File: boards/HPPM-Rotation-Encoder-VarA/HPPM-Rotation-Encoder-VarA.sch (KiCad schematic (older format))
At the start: 13 parts, among them J1 CONN, U1 AS5045B, U2 DS9638

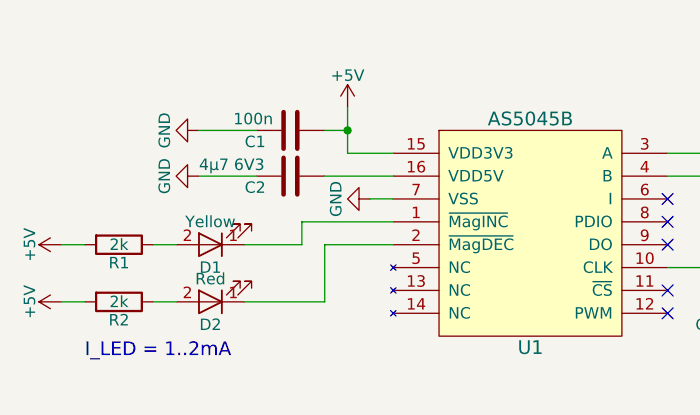
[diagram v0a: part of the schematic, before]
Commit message: [board][HPPM-Rotation-Encoder-VarA] fix wrong pinout
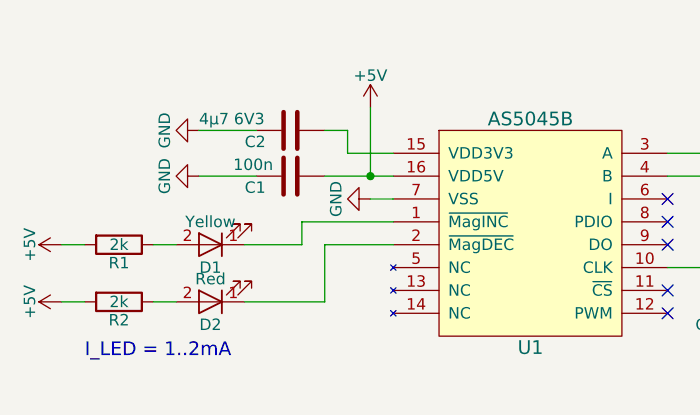
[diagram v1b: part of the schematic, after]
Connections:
- net +5V: now also U1.16 (VDD5V); no longer U1.15 (VDD3V3)
- net at C2.1: now also U1.15 (VDD3V3); no longer U1.16 (VDD5V)
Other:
- moved on the sheet: C1, C2
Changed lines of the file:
@@
 LIBS:ds9638
 LIBS:as5045b
+LIBS:HPPM-Rotation-Encoder-VarA-cache
 EELAYER 25 0
 EELAYER END
@@
 L +5V #PWR01
 U 1 1 5B107E82
-P 4800 3150
-F 0 "#PWR01" H 4800 3000 50  0001 C CNN
-F 1 "+5V" H 4800 3290 50  0000 C CNN
-F 2 "" H 4800 3150 50  0001 C CNN
-F 3 "" H 4800 3150 50  0001 C CNN
-	1    4800 3150
-	1    0    0    -1
-$EndComp
-Wire Wire Line
-	5000 3350 4800 3350
-Wire Wire Line
-	4800 3350 4800 3150
+P 4900 3150
+F 0 "#PWR01" H 4900 3000 50  0001 C CNN
+F 1 "+5V" H 4900 3290 50  0000 C CNN
+F 2 "" H 4900 3150 50  0001 C CNN
+F 3 "" H 4900 3150 50  0001 C CNN
+	1    4900 3150
+	1    0    0    -1
+$EndComp
 $Comp
 L GND #PWR02
@@
 L C C1
 U 1 1 5B107F98
+P 4550 3450
+F 0 "C1" V 4600 3250 50  0000 L CNN
+F 1 "100n" V 4500 3200 50  0000 L CNN
+F 2 "Capacitors_SMD:C_0603" H 4588 3300 50  0001 C CNN
+F 3 "" H 4550 3450 50  0001 C CNN
+	1    4550 3450
+	0    1    1    0
+$EndComp
+$Comp
+L GND #PWR03
+U 1 1 5B1080A9
+P 4150 3450
+F 0 "#PWR03" H 4150 3200 50  0001 C CNN
+F 1 "GND" H 4150 3300 50  0000 C CNN
+F 2 "" H 4150 3450 50  0001 C CNN
+F 3 "" H 4150 3450 50  0001 C CNN
+	1    4150 3450
+	0    1    1    0
+$EndComp
+Wire Wire Line
+	4900 3550 5000 3550
+$Comp
+L C C2
+U 1 1 5B1080D6
 P 4550 3250
-F 0 "C1" V 4600 3050 50  0000 L CNN
-F 1 "100n" V 4500 3000 50  0000 L CNN
+F 0 "C2" V 4600 3050 50  0000 L CNN
+F 1 "4µ7 6V3" V 4500 2850 50  0000 L CNN
 F 2 "Capacitors_SMD:C_0603" H 4588 3100 50  0001 C CNN
 F 3 "" H 4550 3250 50  0001 C CNN
@@
 $EndComp
 $Comp
-L GND #PWR03
-U 1 1 5B1080A9
+L GND #PWR04
+U 1 1 5B10817D
 P 4150 3250
-F 0 "#PWR03" H 4150 3000 50  0001 C CNN
+F 0 "#PWR04" H 4150 3000 50  0001 C CNN
 F 1 "GND" H 4150 3100 50  0000 C CNN
 F 2 "" H 4150 3250 50  0001 C CNN
@@
 $EndComp
 Wire Wire Line
-	4900 3550 5000 3550
-$Comp
-L C C2
-U 1 1 5B1080D6
-P 4550 3450
-F 0 "C2" V 4600 3250 50  0000 L CNN
-F 1 "4µ7 6V3" V 4500 3050 50  0000 L CNN
-F 2 "Capacitors_SMD:C_0603" H 4588 3300 50  0001 C CNN
-F 3 "" H 4550 3450 50  0001 C CNN
-	1    4550 3450
-	0    1    1    0
-$EndComp
-$Comp
-L GND #PWR04
-U 1 1 5B10817D
-P 4150 3450
-F 0 "#PWR04" H 4150 3200 50  0001 C CNN
-F 1 "GND" H 4150 3300 50  0000 C CNN
-F 2 "" H 4150 3450 50  0001 C CNN
-F 3 "" H 4150 3450 50  0001 C CNN
-	1    4150 3450
-	0    1    1    0
-$EndComp
+	4150 3250 4400 3250
 Wire Wire Line
 	4150 3450 4400 3450
-Wire Wire Line
-	4150 3250 4400 3250
-Wire Wire Line
-	4700 3250 4800 3250
-Connection ~ 4800 3250
-Wire Wire Line
-	4700 3450 5000 3450
 $Comp
 L C C4
@@
 Wire Wire Line
 	9250 3050 9250 2950
+Wire Wire Line
+	4700 3450 5000 3450
+Wire Wire Line
+	5000 3350 4800 3350
+Wire Wire Line
+	4800 3350 4800 3250
+Wire Wire Line
+	4800 3250 4700 3250
+Wire Wire Line
+	4900 3150 4900 3450
+Connection ~ 4900 3450
 $EndSCHEMATC

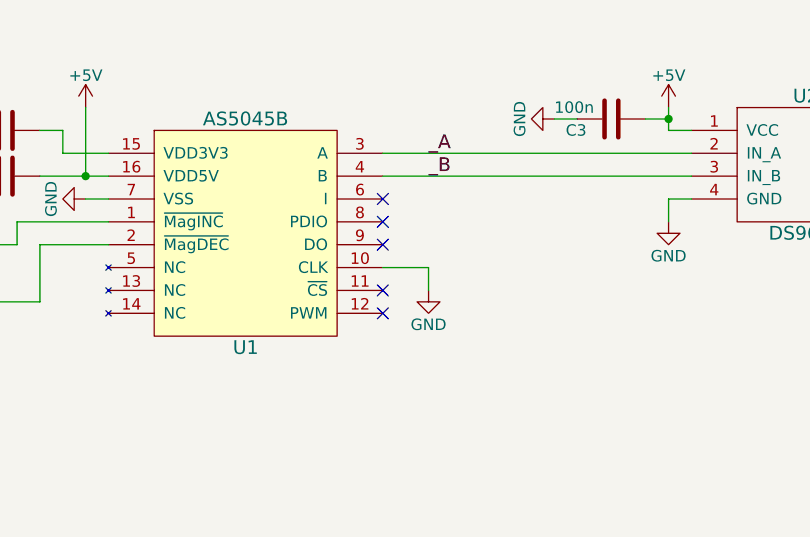
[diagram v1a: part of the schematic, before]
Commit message: [board][HPPM-Rotation-Encoder-Var*] minor fiixes: DRC and PDIO wired to GND
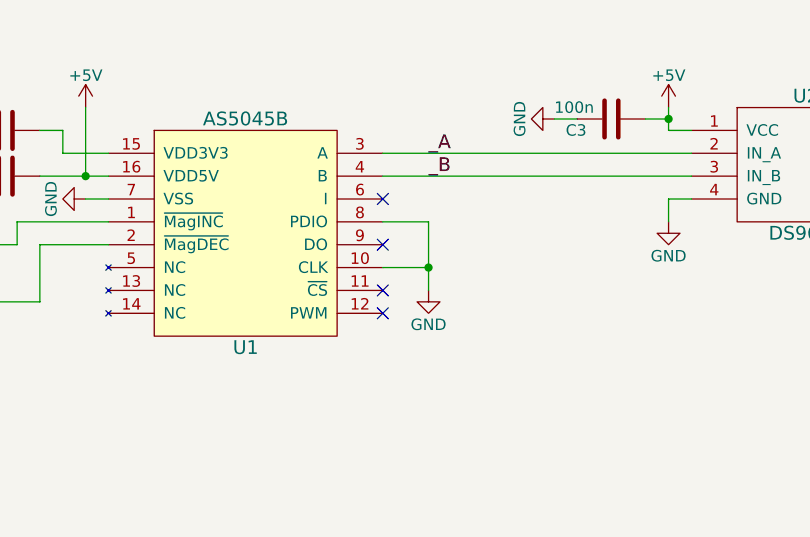
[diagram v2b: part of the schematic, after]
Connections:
- net GND: now also U1.8 (PDIO)
- no-connect marks 5 -> 4
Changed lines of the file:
@@
 NoConn ~ 6200 3550
 NoConn ~ 6200 3750
-NoConn ~ 6200 3650
 $Comp
 L GND #PWR015
@@
 $EndComp
 Wire Wire Line
-	6400 3950 6400 3850
+	6400 3650 6400 3950
 Wire Wire Line
 	6400 3850 6200 3850
@@
 	4900 3150 4900 3450
 Connection ~ 4900 3450
+Wire Wire Line
+	6200 3650 6400 3650
+Connection ~ 6400 3850
 $EndSCHEMATC
